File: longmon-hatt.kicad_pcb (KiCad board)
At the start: 2 copper layers, 67.5 x 36 mm, 4 parts

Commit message: Finalize PCB for ordering
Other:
- board text added: "Designed by Carson Bush & Dylan Hansen"
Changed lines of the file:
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@@
       (plot_on_all_layers_selection 0x0000000_00000000)
       (disableapertmacros false)
-      (usegerberextensions false)
-      (usegerberattributes true)
-      (usegerberadvancedattributes true)
-      (creategerberjobfile true)
+      (usegerberextensions true)
+      (usegerberattributes false)
+      (usegerberadvancedattributes false)
+      (creategerberjobfile false)
       (dashed_line_dash_ratio 12.000000)
       (dashed_line_gap_ratio 3.000000)
@@
       (psa4output false)
       (plotreference true)
-      (plotvalue true)
+      (plotvalue false)
       (plotinvisibletext false)
       (sketchpadsonfab false)
-      (subtractmaskfromsilk false)
+      (subtractmaskfromsilk true)
       (outputformat 1)
       (mirror false)
-      (drillshape 1)
+      (drillshape 0)
       (scaleselection 1)
-      (outputdirectory "")
+      (outputdirectory "gerber/")
     )
   )
@@
   (gr_rect (start 128.5 79) (end 196 115)
     (stroke (width 0.1) (type default)) (fill none) (layer "Edge.Cuts"))
+  (gr_text "Designed by Carson Bush & Dylan Hansen" (at 189 82) (layer "B.SilkS")
+    (effects (font (size 1 1) (thickness 0.15)) (justify left bottom mirror))
+  )
+  (gr_text_box "But, behold, Zion hath said: The Lord hath forsaken me, and my Lord hath forgotten me-but he will show that he hath not.\n\n1 Nephi 21:14"
+    (start 154.5 92) (end 181.5 103) (layer "B.SilkS")
+      (effects (font (size 1 1) (thickness 0.15) italic) (justify left top mirror))
+    (stroke (width 0.15) (type solid))  )
   (segment (start 129.8842 97.3842) (end 129.8842 91.1158) (width 0.25) (layer "B.Cu") (net 1))
   (segment (start 135 102.5) (end 129.8842 97.3842) (width 0.25) (layer "B.Cu") (net 1))

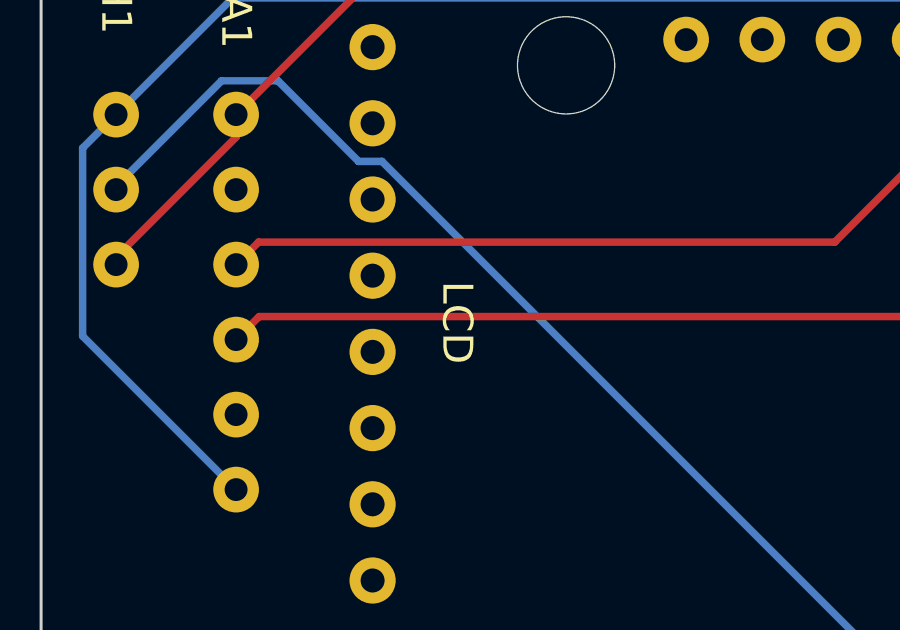
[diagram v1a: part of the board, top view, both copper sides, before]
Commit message: Fixed LCD pins not being connected bug
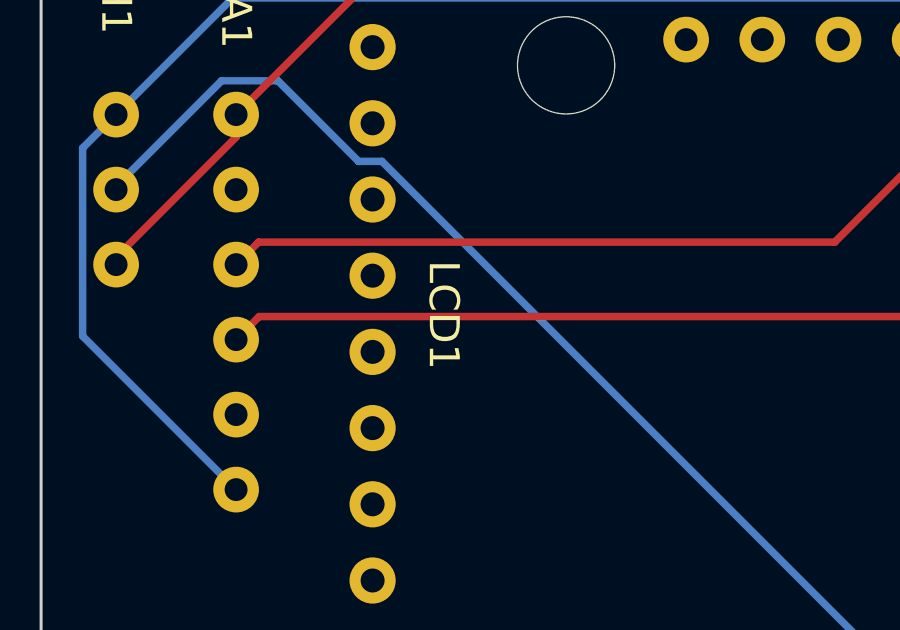
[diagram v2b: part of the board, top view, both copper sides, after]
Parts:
- removed LCD: LCD Module, ESP:LCD Module
- added LCD1: ~, ESP:LCD Module, F.Cu at (139.6, 81.6)
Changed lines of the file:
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@@
       (net 1 "Net-(LCD1-VCC)") (pinfunction "VDD") (pintype "power_in"))
   )
+  (footprint "ESP:POT Header" (layer "F.Cu")
+    (at 131 90)
+    (property "Sheetfile" "longmon-hatt.kicad_sch")
+    (property "Sheetname" "")
+    (property "Sim.Enable" "0")
+    (attr through_hole)
+    (fp_text reference "POTH1" (at 0 -5 270 unlocked) (layer "F.SilkS")
+        (effects (font (size 1 1) (thickness 0.153)))
+    )
+    (fp_text value "~" (at 7.5 1.5 unlocked) (layer "F.Fab") hide
+        (effects (font (size 1 1) (thickness 0.15)))
+    )
+    (fp_text user "${REFERENCE}" (at 7.5 3 unlocked) (layer "F.Fab") hide
+        (effects (font (size 1 1) (thickness 0.15)))
+    )
+    (pad "DIV" thru_hole circle (at 0 2.5) (size 1.524 1.524) (drill 0.762) (layers "*.Cu" "*.Mask")
+      (net 5 "Net-(ESPH1-D34)") (pinfunction "DIV") (pintype "output"))
+    (pad "GND" thru_hole circle (at 0 5) (size 1.524 1.524) (drill 0.762) (layers "*.Cu" "*.Mask")
+      (net 28 "Net-(LCD1-GND)") (pinfunction "GND") (pintype "power_in"))
+    (pad "VCC" thru_hole circle (at 0 0) (size 1.524 1.524) (drill 0.762) (layers "*.Cu" "*.Mask")
+      (net 1 "Net-(LCD1-VCC)") (pinfunction "VCC") (pintype "power_in"))
+  )
   (footprint "ESP:LCD Module" (layer "F.Cu")
     (at 139.55 81.64)
+    (property "Sheetfile" "longmon-hatt.kicad_sch")
+    (property "Sheetname" "")
+    (property "Sim.Enable" "0")
     (attr through_hole)
-    (fp_text reference "LCD" (at 2.82 15.29 -90 unlocked) (layer "F.SilkS")
+    (fp_text reference "LCD1" (at 2.37 15.04 -90 unlocked) (layer "F.SilkS")
         (effects (font (size 1 1) (thickness 0.153)))
     )
-    (fp_text value "LCD Module" (at 22.86 -9.12 unlocked) (layer "F.Fab") hide
+    (fp_text value "~" (at 22.86 -9.12 unlocked) (layer "F.Fab") hide
         (effects (font (size 1 1) (thickness 0.15)))
     )
@@
       )
     )
-    (fp_text user "${REFERENCE}" (at 2.82 15.29 -90 unlocked) (layer "F.Fab")
+    (fp_text user "${REFERENCE}" (at 2.37 15.04 -90 unlocked) (layer "F.Fab")
         (effects (font (size 1 1) (thickness 0.15)))
     )
@@
     (pad "" np_thru_hole circle (at 0 30) (size 3 3) (drill 2) (layers "F&B.Cu" "*.Mask"))
     (pad "" np_thru_hole circle (at 53 0) (size 3 3) (drill 2) (layers "F&B.Cu" "*.Mask"))
-    (pad "1" thru_hole circle (at 0 6.11) (size 1.54 1.54) (drill 0.8) (layers "*.Cu" "*.Mask"))
-    (pad "2" thru_hole circle (at 0 8.65) (size 1.54 1.54) (drill 0.8) (layers "*.Cu" "*.Mask"))
-    (pad "3" thru_hole circle (at 0 11.19) (size 1.54 1.54) (drill 0.8) (layers "*.Cu" "*.Mask"))
-    (pad "4" thru_hole circle (at 0 13.73) (size 1.54 1.54) (drill 0.8) (layers "*.Cu" "*.Mask"))
-    (pad "5" thru_hole circle (at 0 16.27) (size 1.54 1.54) (drill 0.8) (layers "*.Cu" "*.Mask"))
-    (pad "6" thru_hole circle (at 0 18.81) (size 1.54 1.54) (drill 0.8) (layers "*.Cu" "*.Mask"))
-    (pad "7" thru_hole circle (at 0 21.35) (size 1.54 1.54) (drill 0.8) (layers "*.Cu" "*.Mask"))
-    (pad "8" thru_hole circle (at 0 23.89) (size 1.54 1.54) (drill 0.8) (layers "*.Cu" "*.Mask"))
-  )
-  (footprint "ESP:POT Header" (layer "F.Cu")
-    (at 131 90)
-    (property "Sheetfile" "longmon-hatt.kicad_sch")
-    (property "Sheetname" "")
-    (property "Sim.Enable" "0")
-    (attr through_hole)
-    (fp_text reference "POTH1" (at 0 -5 270 unlocked) (layer "F.SilkS")
-        (effects (font (size 1 1) (thickness 0.153)))
-    )
-    (fp_text value "~" (at 7.5 1.5 unlocked) (layer "F.Fab") hide
-        (effects (font (size 1 1) (thickness 0.15)))
-    )
-    (fp_text user "${REFERENCE}" (at 7.5 3 unlocked) (layer "F.Fab") hide
-        (effects (font (size 1 1) (thickness 0.15)))
-    )
-    (pad "DIV" thru_hole circle (at 0 2.5) (size 1.524 1.524) (drill 0.762) (layers "*.Cu" "*.Mask")
-      (net 5 "Net-(ESPH1-D34)") (pinfunction "DIV") (pintype "output"))
-    (pad "GND" thru_hole circle (at 0 5) (size 1.524 1.524) (drill 0.762) (layers "*.Cu" "*.Mask")
-      (net 28 "Net-(LCD1-GND)") (pinfunction "GND") (pintype "power_in"))
-    (pad "VCC" thru_hole circle (at 0 0) (size 1.524 1.524) (drill 0.762) (layers "*.Cu" "*.Mask")
+    (pad "1" thru_hole circle (at 0 6.11) (size 1.54 1.54) (drill 0.8) (layers "*.Cu" "*.Mask")
       (net 1 "Net-(LCD1-VCC)") (pinfunction "VCC") (pintype "power_in"))
+    (pad "2" thru_hole circle (at 0 8.65) (size 1.54 1.54) (drill 0.8) (layers "*.Cu" "*.Mask")
+      (net 28 "Net-(LCD1-GND)") (pinfunction "GND") (pintype "power_in"))
+    (pad "3" thru_hole circle (at 0 11.19) (size 1.54 1.54) (drill 0.8) (layers "*.Cu" "*.Mask")
+      (net 22 "Net-(ESPH1-D23)") (pinfunction "DIN") (pintype "input"))
+    (pad "4" thru_hole circle (at 0 13.73) (size 1.54 1.54) (drill 0.8) (layers "*.Cu" "*.Mask")
+      (net 21 "Net-(ESPH1-D18)") (pinfunction "CLK") (pintype "input"))
+    (pad "5" thru_hole circle (at 0 16.27) (size 1.54 1.54) (drill 0.8) (layers "*.Cu" "*.Mask")
+      (net 20 "Net-(ESPH1-D5)") (pinfunction "CS") (pintype "input"))
+    (pad "6" thru_hole circle (at 0 18.81) (size 1.54 1.54) (drill 0.8) (layers "*.Cu" "*.Mask")
+      (net 23 "Net-(ESPH1-D19)") (pinfunction "DC") (pintype "input"))
+    (pad "7" thru_hole circle (at 0 21.35) (size 1.54 1.54) (drill 0.8) (layers "*.Cu" "*.Mask")
+      (net 17 "Net-(ESPH1-D4)") (pinfunction "RST") (pintype "input"))
+    (pad "8" thru_hole circle (at 0 23.89) (size 1.54 1.54) (drill 0.8) (layers "*.Cu" "*.Mask")
+      (net 27 "Net-(ESPH1-D21)") (pinfunction "BL") (pintype "input"))
   )
   (gr_rect (start 128.5 79) (end 196 115)
     (stroke (width 0.1) (type default)) (fill none) (layer "Edge.Cuts"))
   (gr_text "Designed by Carson Bush & Dylan Hansen" (at 189 82) (layer "B.SilkS")
-    (effects (font (size 1 1) (thickness 0.15)) (justify left bottom mirror))
+    (effects (font (size 1 1) (thickness 0.153)) (justify left bottom mirror))
   )
   (gr_text_box "But, behold, Zion hath said: The Lord hath forsaken me, and my Lord hath forgotten me-but he will show that he hath not.\n\n1 Nephi 21:14"
     (start 154.5 92) (end 181.5 103) (layer "B.SilkS")
-      (effects (font (size 1 1) (thickness 0.15) italic) (justify left top mirror))
+      (effects (font (size 1 1) (thickness 0.153) italic) (justify left top mirror))
     (stroke (width 0.15) (type solid))  )
   (segment (start 129.8842 97.3842) (end 129.8842 91.1158) (width 0.25) (layer "B.Cu") (net 1))

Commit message: Autorouted traces
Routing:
- net Net-(ESPH1-D4): track 0.00 -> 42.3 mm
- net Net-(ESPH1-D5): track 0.00 -> 32.5 mm
- net Net-(ESPH1-D19): track 0.00 -> 29.8 mm
- net Net-(ESPH1-D18): track 0.00 -> 28.9 mm
- net Net-(ESPH1-D21): track 0.00 -> 28.1 mm
- net Net-(ESPH1-D23): track 0.00 -> 12.7 mm
- net Net-(ESPH1-TX2): track 39.5 -> 40.7 mm
- net Net-(ESPH1-D34): track 39.8 -> 38.8 mm
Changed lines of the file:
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@@
       (effects (font (size 1 1) (thickness 0.153) italic) (justify left top mirror))
     (stroke (width 0.15) (type solid))  )
-  (segment (start 129.8842 97.3842) (end 129.8842 91.1158) (width 0.25) (layer "B.Cu") (net 1))
-  (segment (start 135 102.5) (end 129.8842 97.3842) (width 0.25) (layer "B.Cu") (net 1))
-  (segment (start 131 90) (end 134.8886 86.1114) (width 0.25) (layer "B.Cu") (net 1))
-  (segment (start 129.8842 91.1158) (end 131 90) (width 0.25) (layer "B.Cu") (net 1))
-  (segment (start 184.1714 86.1114) (end 185.56 87.5) (width 0.25) (layer "B.Cu") (net 1))
-  (segment (start 134.8886 86.1114) (end 184.1714 86.1114) (width 0.25) (layer "B.Cu") (net 1))
-  (segment (start 157.62 109.3175) (end 157.62 112.5) (width 0.25) (layer "B.Cu") (net 5))
-  (segment (start 134.514 88.8739) (end 136.3937 88.8739) (width 0.25) (layer "B.Cu") (net 5))
-  (segment (start 139.8625 91.56) (end 157.62 109.3175) (width 0.25) (layer "B.Cu") (net 5))
-  (segment (start 131 92.3879) (end 134.514 88.8739) (width 0.25) (layer "B.Cu") (net 5))
-  (segment (start 139.0798 91.56) (end 139.8625 91.56) (width 0.25) (layer "B.Cu") (net 5))
-  (segment (start 136.3937 88.8739) (end 139.0798 91.56) (width 0.25) (layer "B.Cu") (net 5))
-  (segment (start 131 92.5) (end 131 92.3879) (width 0.25) (layer "B.Cu") (net 5))
-  (segment (start 162.2121 86.3979) (end 171.7557 86.3979) (width 0.25) (layer "F.Cu") (net 18))
-  (segment (start 135.749 94.251) (end 154.9559 94.251) (width 0.25) (layer "F.Cu") (net 18))
-  (segment (start 135 95) (end 135.749 94.251) (width 0.25) (layer "F.Cu") (net 18))
-  (segment (start 171.9791 86.6213) (end 171.9813 86.6213) (width 0.25) (layer "F.Cu") (net 18))
-  (segment (start 161.43 87.18) (end 162.2121 86.3979) (width 0.25) (layer "F.Cu") (net 18))
-  (segment (start 161.43 87.7769) (end 161.43 87.18) (width 0.25) (layer "F.Cu") (net 18))
-  (segment (start 171.7557 86.3979) (end 171.9791 86.6213) (width 0.25) (layer "F.Cu") (net 18))
-  (segment (start 171.9813 86.6213) (end 172.86 87.5) (width 0.25) (layer "F.Cu") (net 18))
-  (segment (start 154.9559 94.251) (end 161.43 87.7769) (width 0.25) (layer "F.Cu") (net 18))
-  (segment (start 135.7684 96.7316) (end 161.0884 96.7316) (width 0.25) (layer "F.Cu") (net 19))
-  (segment (start 135 97.5) (end 135.7684 96.7316) (width 0.25) (layer "F.Cu") (net 19))
-  (segment (start 161.0884 96.7316) (end 170.32 87.5) (width 0.25) (layer "F.Cu") (net 19))
-  (segment (start 139.0639 85.9361) (end 181.4561 85.9361) (width 0.25) (layer "F.Cu") (net 28))
-  (segment (start 131 95) (end 131 94.7509) (width 0.25) (layer "F.Cu") (net 28))
-  (segment (start 181.4561 85.9361) (end 183.02 87.5) (width 0.25) (layer "F.Cu") (net 28))
-  (segment (start 131 94.7509) (end 135 90.7509) (width 0.25) (layer "F.Cu") (net 28))
-  (segment (start 135 90) (end 139.0639 85.9361) (width 0.25) (layer "F.Cu") (net 28))
-  (segment (start 135 90.7509) (end 135 90) (width 0.25) (layer "F.Cu") (net 28))
+  (segment (start 139.55 87.75) (end 141.8518 85.4482) (width 0.25) (layer "F.Cu") (net 1))
+  (segment (start 183.5082 85.4482) (end 185.56 87.5) (width 0.25) (layer "F.Cu") (net 1))
+  (segment (start 141.8518 85.4482) (end 183.5082 85.4482) (width 0.25) (layer "F.Cu") (net 1))
+  (segment (start 137.2475 87.75) (end 139.55 87.75) (width 0.25) (layer "B.Cu") (net 1))
+  (segment (start 136.0917 88.9058) (end 137.2475 87.75) (width 0.25) (layer "B.Cu") (net 1))
+  (segment (start 135 102.5) (end 136.0917 101.4083) (width 0.25) (layer "B.Cu") (net 1))
+  (segment (start 132.0942 88.9058) (end 131 90) (width 0.25) (layer "B.Cu") (net 1))
+  (segment (start 136.0917 88.9058) (end 132.0942 88.9058) (width 0.25) (layer "B.Cu") (net 1))
+  (segment (start 136.0917 101.4083) (end 136.0917 88.9058) (width 0.25) (layer "B.Cu") (net 1))
+  (segment (start 149.38 104.26) (end 157.62 112.5) (width 0.25) (layer "F.Cu") (net 5))
+  (segment (start 131 92.5) (end 129.8405 93.6595) (width 0.25) (layer "F.Cu") (net 5))
+  (segment (start 138.3629 104.26) (end 149.38 104.26) (width 0.25) (layer "F.Cu") (net 5))
+  (segment (start 129.8405 96.426) (end 134.6645 101.25) (width 0.25) (layer "F.Cu") (net 5))
+  (segment (start 129.8405 93.6595) (end 129.8405 96.426) (width 0.25) (layer "F.Cu") (net 5))
+  (segment (start 135.3529 101.25) (end 138.3629 104.26) (width 0.25) (layer "F.Cu") (net 5))
+  (segment (start 134.6645 101.25) (end 135.3529 101.25) (width 0.25) (layer "F.Cu") (net 5))
+  (segment (start 139.55 102.99) (end 159.91 102.99) (width 0.25) (layer "F.Cu") (net 17))
+  (segment (start 159.91 102.99) (end 175.4 87.5) (width 0.25) (layer "F.Cu") (net 17))
+  (segment (start 171.2859 85.9259) (end 172.86 87.5) (width 0.25) (layer "F.Cu") (net 18))
+  (segment (start 138.2746 91.7254) (end 149.8607 91.7254) (width 0.25) (layer "F.Cu") (net 18))
+  (segment (start 155.1008 85.9259) (end 171.2859 85.9259) (width 0.25) (layer "F.Cu") (net 18))
+  (segment (start 149.8607 91.7254) (end 153.81 87.7761) (width 0.25) (layer "F.Cu") (net 18))
+  (segment (start 153.81 87.7761) (end 153.81 87.2167) (width 0.25) (layer "F.Cu") (net 18))
+  (segment (start 153.81 87.2167) (end 155.1008 85.9259) (width 0.25) (layer "F.Cu") (net 18))
+  (segment (start 135 95) (end 138.2746 91.7254) (width 0.25) (layer "F.Cu") (net 18))
+  (segment (start 169.2179 86.3979) (end 170.32 87.5) (width 0.25) (layer "F.Cu") (net 19))
+  (segment (start 152.5661 94.1) (end 158.89 87.7761) (width 0.25) (layer "F.Cu") (net 19))
+  (segment (start 135 97.5) (end 138.4 94.1) (width 0.25) (layer "F.Cu") (net 19))
+  (segment (start 138.4 94.1) (end 152.5661 94.1) (width 0.25) (layer "F.Cu") (net 19))
+  (segment (start 159.6717 86.3979) (end 169.2179 86.3979) (width 0.25) (layer "F.Cu") (net 19))
+  (segment (start 158.89 87.1796) (end 159.6717 86.3979) (width 0.25) (layer "F.Cu") (net 19))
+  (segment (start 158.89 87.7761) (end 158.89 87.1796) (width 0.25) (layer "F.Cu") (net 19))
+  (segment (start 157.37 97.91) (end 167.78 87.5) (width 0.25) (layer "F.Cu") (net 20))
+  (segment (start 139.55 97.91) (end 157.37 97.91) (width 0.25) (layer "F.Cu") (net 20))
+  (segment (start 139.55 95.37) (end 157.37 95.37) (width 0.25) (layer "F.Cu") (net 21))
+  (segment (start 157.37 95.37) (end 165.24 87.5) (width 0.25) (layer "F.Cu") (net 21))
+  (segment (start 139.55 92.83) (end 144.67 92.83) (width 0.25) (layer "B.Cu") (net 22))
+  (segment (start 144.67 92.83) (end 150 87.5) (width 0.25) (layer "B.Cu") (net 22))
+  (segment (start 159.6638 86.4068) (end 161.6068 86.4068) (width 0.25) (layer "B.Cu") (net 23))
+  (segment (start 159.0686 87.5914) (end 159.0686 87.002) (width 0.25) (layer "B.Cu") (net 23))
+  (segment (start 139.55 100.45) (end 146.21 100.45) (width 0.25) (layer "B.Cu") (net 23))
+  (segment (start 161.6068 86.4068) (end 162.7 87.5) (width 0.25) (layer "B.Cu") (net 23))
+  (segment (start 159.0686 87.002) (end 159.6638 86.4068) (width 0.25) (layer "B.Cu") (net 23))
+  (segment (start 146.21 100.45) (end 159.0686 87.5914) (width 0.25) (layer "B.Cu") (net 23))
+  (segment (start 139.55 105.53) (end 142.13 105.53) (width 0.25) (layer "B.Cu") (net 27))
+  (segment (start 142.13 105.53) (end 160.16 87.5) (width 0.25) (layer "B.Cu") (net 27))
+  (segment (start 139.55 90.29) (end 135.29 90.29) (width 0.25) (layer "F.Cu") (net 28))
+  (segment (start 135.29 90.29) (end 135 90) (width 0.25) (layer "F.Cu") (net 28))
+  (segment (start 135.29 90.29) (end 131 94.58) (width 0.25) (layer "F.Cu") (net 28))
+  (segment (start 131 94.58) (end 131 95) (width 0.25) (layer "F.Cu") (net 28))
+  (segment (start 181.4499 85.9299) (end 183.02 87.5) (width 0.25) (layer "B.Cu") (net 28))
+  (segment (start 143.9101 85.9299) (end 181.4499 85.9299) (width 0.25) (layer "B.Cu") (net 28))
+  (segment (start 139.55 90.29) (end 143.9101 85.9299) (width 0.25) (layer "B.Cu") (net 28))
   (segment (start 183.02 87.5) (end 183.02 112.5) (width 0.25) (layer "B.Cu") (net 28))
 )
